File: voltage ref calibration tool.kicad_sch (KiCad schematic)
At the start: 66 parts, among them J1 Molex-MicroFit_43650-0316, J2 AudioJack2_SwitchT, J3 Conn_01x02, J4 Conn_01x02, J5 AudioJack2_SwitchT, SW1 SW_SP6T, SW2 B3F-1020, SW3 B3F-1020, SW4 B3F-1020, SW5 B3F-1020, SW6 B3F-1020, U1 TL074H

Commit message: Reset annotations.
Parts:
- renumbered C6 to C1, C1 to C2, C2 to C5, C5 to C6, J5 to J1, J1 to J2, J2 to J3, J3 to J4, J4 to J5, R7 to R1, R6 to R10, R12 to R11, R13 to R12, R14 to R13, R15 to R14, R16 to R15, R29 to R16, R8 to R17, R17 to R18, R18 to R19, R10 to R2, R19 to R20, R20 to R21, R25 to R22, R9 to R23, R21 to R24, R22 to R25, R24 to R27, R27 to R28, R23 to R29, R28 to R3, R1 to R4, R11 to R5, R2 to R6, R3 to R7, R4 to R8, R5 to R9, TP10 to TP1, TP9 to TP10, TP4 to TP2, TP7 to TP3, TP5 to TP4, TP8 to TP5, TP1 to TP7, TP2 to TP8, TP3 to TP9
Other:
- note added: "Adjust trim until TP4 is 5.000 V"
- note removed: "Adjust trim until TP8 is 5.000 V"

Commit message: improve net names.
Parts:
- added R30: 2k2, Resistor_SMD:R_0805_2012Metric_Pad1.20x1.40mm_HandSolder, symbol Device:R_Small
- added TP11: TP, Aaron_Pads:TP_HeaderPin_P2.54mm_round, symbol Connector:TestPoint_Small
- J1, J3: footprint Aaron_THT:Schurter-4832.2211 -> Aaron_Connector:Schurter-4832.2211
- J2: footprint Aaron_THT:Molex-Microfit-43650-0316 -> Aaron_Connector:Molex-Microfit-43650-0316
- SW1: footprint Aaron_THT:Alpha_SR1712F -> Aaron_Switch:Alpha_SR1712F
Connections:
- net ALT_INV: now also U1.8; no longer U1.14
- net GND: now also U1.3 (+), R30.1; no longer J1.TN, U1.5 (+)
- net OUT: now also TP11.1
- net VGND: now also U1.13 (-); no longer U1.6 (-)
- net VINV: now also U1.14; no longer U1.7
- net VSUM: now also U1.1; no longer U1.8
- net REF5V0A: now reaches R6.1, RV1.2, RV1.3, SW1.7, TP4.1
- net REF6A: now reaches D1.1 (K), R1.2, R4.1, TP2.1
- net REF5V0B: now reaches R11.1, RV2.2, RV2.3, SW2.1, TP5.1
- net REF6B: now reaches D2.1 (K), R2.2, R5.1, TP3.1
- net at R23.2: now also U1.5 (+); no longer U1.3 (+)
- net at C1.1, R16.1, R3.2: now also U1.9 (-); no longer U1.13 (-)
- net at R26.1, R28.1: now also U1.2 (-); no longer U1.9 (-)
- new net: J1.TN, R30.2
- new net: R24.1, U1.6 (-), U1.7
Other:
- moved on the sheet: U1A, U1B, U1C, U1D

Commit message: don't invert alt ref in
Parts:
- removed C1: 33pF, Capacitor_SMD:C_0805_2012Metric_Pad1.18x1.45mm_HandSolder, symbol Device:C_Small
- removed R16: 100k 0.1%, Resistor_SMD:R_0805_2012Metric_Pad1.20x1.40mm_HandSolder, symbol Device:R_Small
- removed R30: 2k2, Resistor_SMD:R_0805_2012Metric_Pad1.20x1.40mm_HandSolder, symbol Device:R_Small
- added TP12: TP, Aaron_Pads:TP_HeaderPin_P2.54mm_round, symbol Connector:TestPoint_Small
- R3: value 100k 0.1% -> 10k; IPN 000052E -> 000049E; IPN, Base 000052E -> 000049; MANUFACTURER Panasonic Electronic Components -> Stackpole; MPN ERA-6AEB104V -> RMCF0805FT10K0
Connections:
- net ALT_V_IN: now also U1.10 (+); no longer R3.1
- net GND: now also R3.1; no longer U1.10 (+)
- net VINV: now also TP12.1
- net at R3.2: now also J1.TN; no longer U1.9 (-)
- net ALT_INV renamed ALT_BUF
- net ALT_BUF: now also U1.9 (-)
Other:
- moved on the sheet: J1, TP1

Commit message: Some final cleanup. Ready to go.
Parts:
- added R16, R30: 47k, Resistor_SMD:R_0805_2012Metric_Pad1.20x1.40mm_HandSolder, symbol Device:R_Small
- added R31: 10k, Resistor_SMD:R_0805_2012Metric_Pad1.20x1.40mm_HandSolder, symbol Device:R_Small
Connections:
- net GND: now also R16.2, R30.2, R31.1; no longer J3.S, U1.12 (+), U1.3 (+)
- net REF5V0A: now also RV1.1; no longer RV1.3
- net REF5V0B: now also RV2.1; no longer RV2.3
- net at R5.2: now also RV2.3; no longer RV2.1
- net at R4.2: now also RV1.3; no longer RV1.1
- new net: R16.1, U1.12 (+)
- new net: R30.1, U1.3 (+)
- new net: J3.S, R31.2
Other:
- moved on the sheet: J4, J5

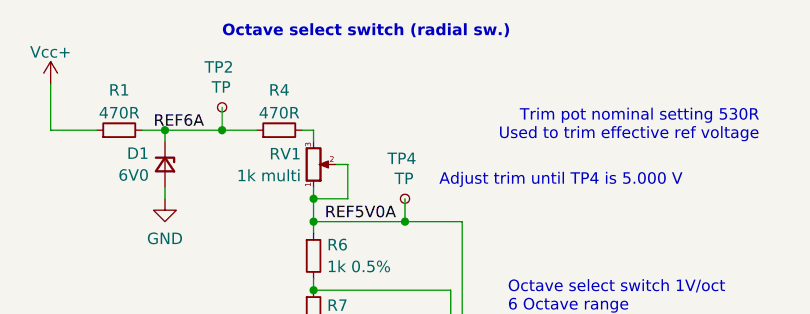
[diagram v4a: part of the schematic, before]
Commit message: Better readme.
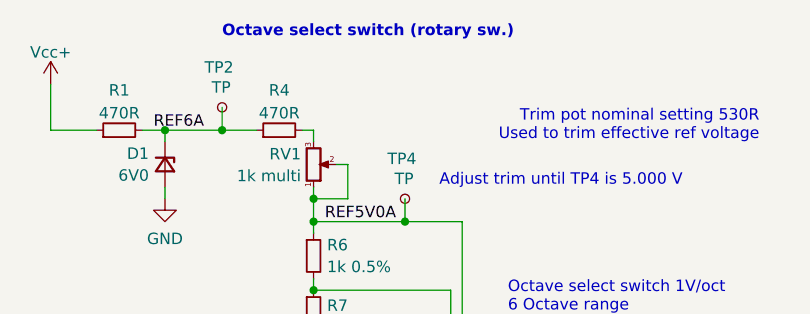
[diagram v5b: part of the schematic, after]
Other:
- note added: "Octave select switch (rotary sw.)"
- note removed: "Octave select switch (radial sw.)"
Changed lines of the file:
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@@
 		)
 	)
-	(text "Octave select switch (radial sw.)"
+	(text "Octave select switch (rotary sw.)"
 		(exclude_from_sim no)
 		(at 43.18 16.51 0)

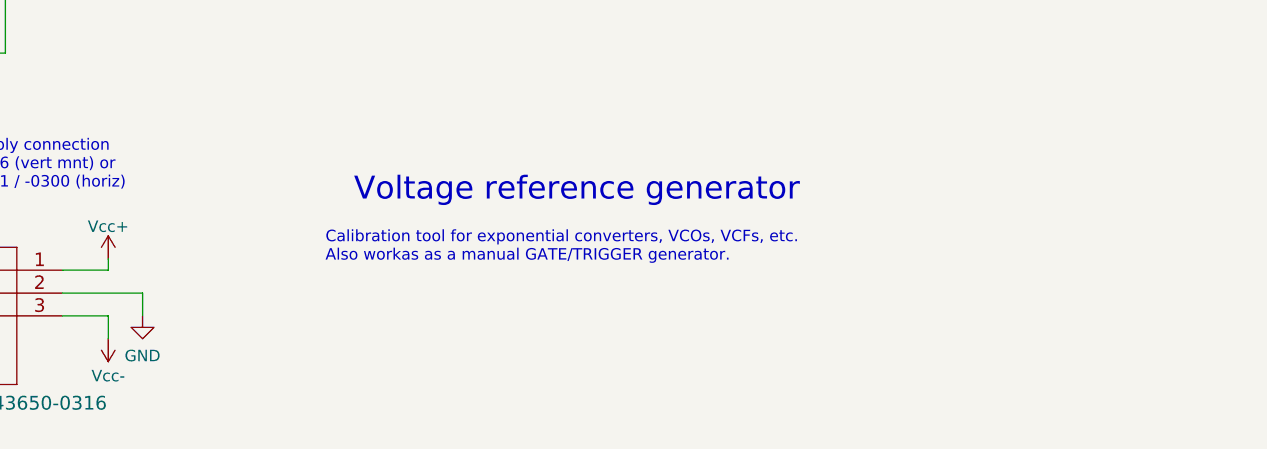
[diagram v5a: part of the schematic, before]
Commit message: Add copyright legend to schematic and pcb.
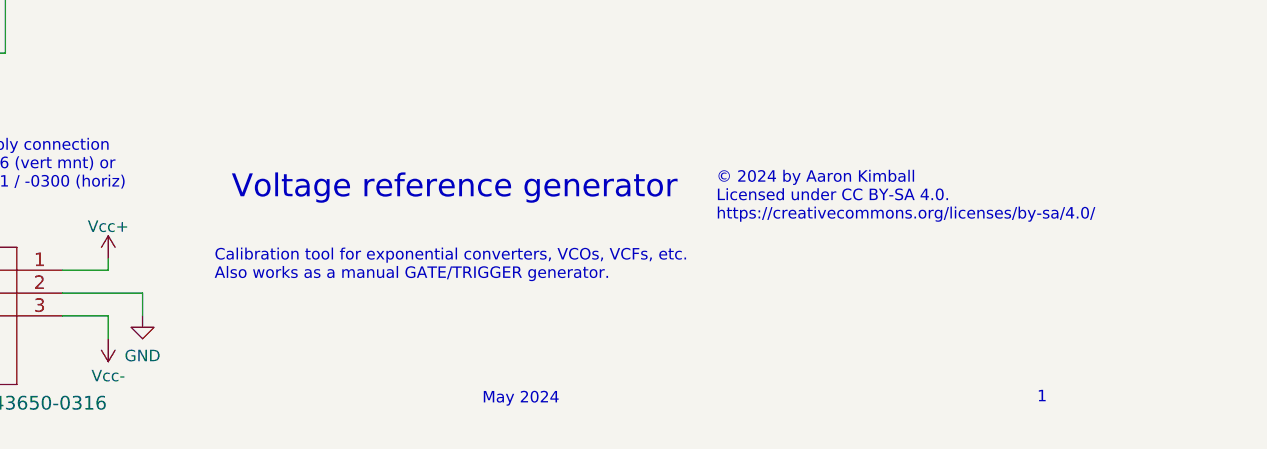
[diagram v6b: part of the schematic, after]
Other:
- note added: "1"
- note added: "Calibration tool for exponential converters, VCOs, VCFs, etc. Also works as a manual GATE/TRIGGER generator."
- note added: "May 2024"
- note added: "© 2024 by Aaron Kimball Licensed under CC BY-SA 4.0. https://creativecommons.org/licenses/by-sa/4.0/"
- note removed: "Calibration tool for exponential converters, VCOs, VCFs, etc. Also workas as a manual GATE/TRIGGER generator."
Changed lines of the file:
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@@
+		)
+	)
+	(text "May 2024"
+		(exclude_from_sim no)
+		(at 212.217 193.421 0)
+		(effects
+			(font
+				(size 1.27 1.27)
+			)
 		)
 	)
@@
 		)
 	)
+	(text "1"
+		(exclude_from_sim no)
+		(at 270.129 193.294 0)
+		(effects
+			(font
+				(size 1.27 1.27)
+			)
+		)
+	)
 	(text "Octave select switch 1V/oct\n6 Octave range\n"
 		(exclude_from_sim no)
@@
 			)
 			(justify left bottom)
+		)
+	)
+	(text "© 2024 by Aaron Kimball\nLicensed under CC BY-SA 4.0.\nhttps://creativecommons.org/licenses/by-sa/4.0/"
+		(exclude_from_sim no)
+		(at 233.934 170.942 0)
+		(effects
+			(font
+				(size 1.27 1.27)
+			)
+			(justify left)
 		)
 	)
@@
 		)
 	)
-	(text "Calibration tool for exponential converters, VCOs, VCFs, etc.\nAlso workas as a manual GATE/TRIGGER generator."
+	(text "Calibration tool for exponential converters, VCOs, VCFs, etc.\nAlso works as a manual GATE/TRIGGER generator."
 		(exclude_from_sim no)
-		(at 190.5 176.53 0)
+		(at 178.181 178.562 0)
 		(effects
 			(font
@@
 	(text "Voltage reference generator"
 		(exclude_from_sim no)
-		(at 218.44 170.18 0)
+		(at 204.851 169.926 0)
 		(effects
 			(font
